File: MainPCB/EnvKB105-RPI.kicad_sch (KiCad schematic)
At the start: 284 parts, among them J2 Button, J5 Conn_01x03_Male, U1 SOT-23-5 5.5V 3.3V 500mA, U3 RP2040, Y1 3225_4P 12MHz

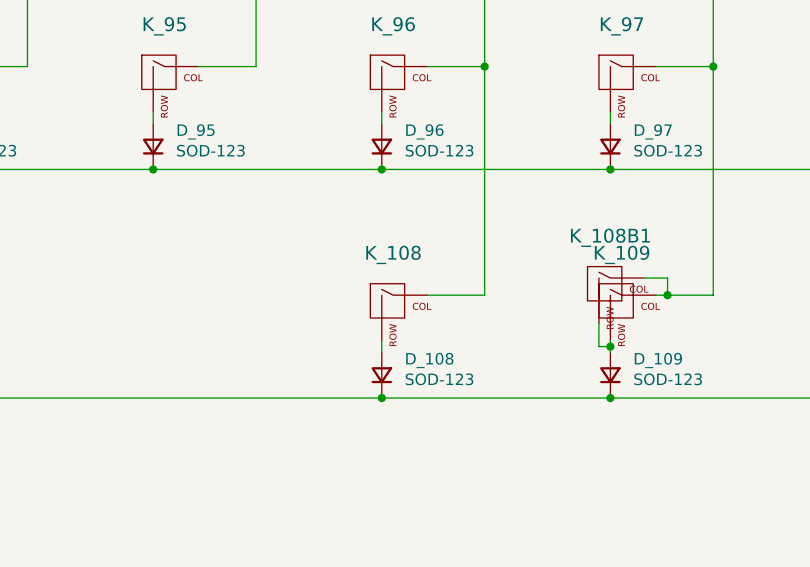
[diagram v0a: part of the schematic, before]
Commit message: Various fixes to clearances and fixed a lot of traces
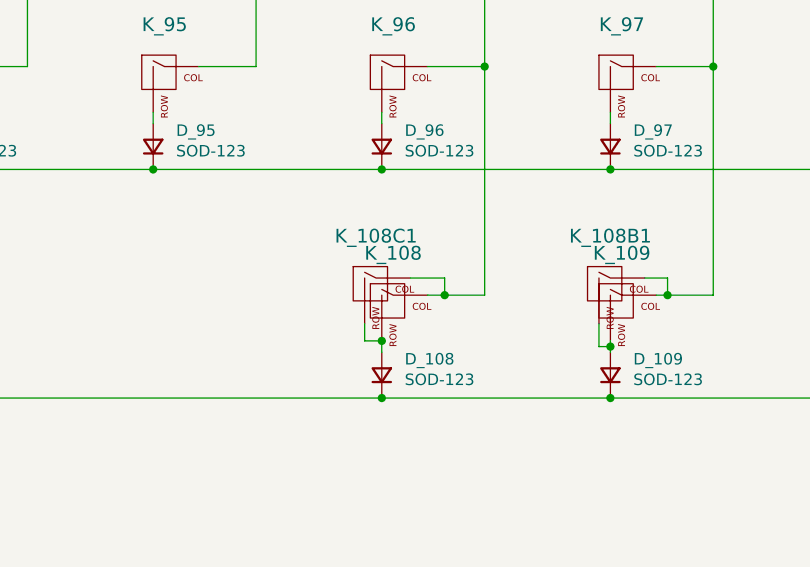
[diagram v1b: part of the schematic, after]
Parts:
- added K_108C1: KEYSW, EnvExtras:MXOnly-1U-Hotswap-Modified, symbol MX_Alps_Hybrid:MX-NoLED
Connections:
- net col10: now also K_108C1.1 (COL)
- net at D_108.2 (A), K_108.2 (ROW): now also K_108C1.2 (ROW)
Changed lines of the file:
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@@
   (junction (at 271.78 60.96) (diameter 0) (color 0 0 0 0)
   )
+  (junction (at 310.515 524.51) (diameter 0) (color 0 0 0 0)
+  )
   (junction (at 289.56 448.31) (diameter 0) (color 0 0 0 0)
   )
@@
   (junction (at 100.33 459.74) (diameter 0) (color 0 0 0 0)
   )
+  (junction (at 303.53 529.59) (diameter 0) (color 0 0 0 0)
+  )
   (junction (at 100.33 485.14) (diameter 0) (color 0 0 0 0)
   )
@@
     (stroke (width 0) (type default))
   )
+  (wire (pts (xy 301.625 529.59) (xy 303.53 529.59))
+    (stroke (width 0) (type default))
+  )
   (wire (pts (xy 557.53 504.19) (xy 557.53 505.46))
     (stroke (width 0) (type default))
@@
     (stroke (width 0) (type default))
   )
+  (wire (pts (xy 310.515 524.51) (xy 314.96 524.51))
+    (stroke (width 0) (type default))
+  )
   (wire (pts (xy 252.73 478.79) (xy 252.73 480.06))
     (stroke (width 0) (type default))
@@
     (stroke (width 0) (type default))
   )
+  (wire (pts (xy 301.625 527.685) (xy 301.625 529.59))
+    (stroke (width 0) (type default))
+  )
   (wire (pts (xy 100.33 377.19) (xy 100.33 378.46))
     (stroke (width 0) (type default))
@@
     (stroke (width 0) (type default))
   )
+  (wire (pts (xy 306.705 522.605) (xy 310.515 522.605))
+    (stroke (width 0) (type default))
+  )
   (wire (pts (xy 80.645 524.51) (xy 86.36 524.51))
     (stroke (width 0) (type default))
@@
     (stroke (width 0) (type default))
   )
+  (wire (pts (xy 310.515 522.605) (xy 310.515 524.51))
+    (stroke (width 0) (type default))
+  )
   (wire (pts (xy 354.33 383.54) (xy 379.73 383.54))
     (stroke (width 0) (type default))
@@
     (stroke (width 0) (type default))
   )
-  (wire (pts (xy 308.61 524.51) (xy 314.96 524.51))
+  (wire (pts (xy 308.61 524.51) (xy 310.515 524.51))
     (stroke (width 0) (type default))
   )
@@
         )
       )
+    )
+  )
+  (symbol (lib_id "MX_Alps_Hybrid:MX-NoLED") (at 302.895 523.875 0) (unit 1)
+    (in_bom yes) (on_board yes) (dnp no)
+    (property "Reference" "K_108C1" (at 302.895 517.9568 0)
+      (effects (font (size 1.524 1.524)))
+    )
+    (property "Value" "KEYSW" (at 302.895 526.415 0)
+      (effects (font (size 1.524 1.524)) hide)
+    )
+    (property "Footprint" "EnvExtras:MXOnly-1U-Hotswap-Modified" (at 302.895 523.875 0)
+      (effects (font (size 1.524 1.524)) hide)
+    )
+    (property "Datasheet" "" (at 302.895 523.875 0)
+      (effects (font (size 1.524 1.524)))
+    )
+    (pin "1")
+    (pin "2")
+    (instances
+      (project "EnvKB105-RPI"
+        (path "/597a11f2-5d2c-4a65-ac95-38ad106e1367"
+          (reference "K_108C1") (unit 1)
+        )
+      )
